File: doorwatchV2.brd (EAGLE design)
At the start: 91.4 x 77.5 mm, 43 parts, among them IC1 LM2576S-5.0, IC2 MAX3232CPE, K1 FINDER-43.61, Q1 IRLZ44Z, T1 BC847, T2 BC847, T3 BC847, T4 BC847, X1 MKDSN1,5/2-5,08, X2 D-SUB9-H2M09RA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

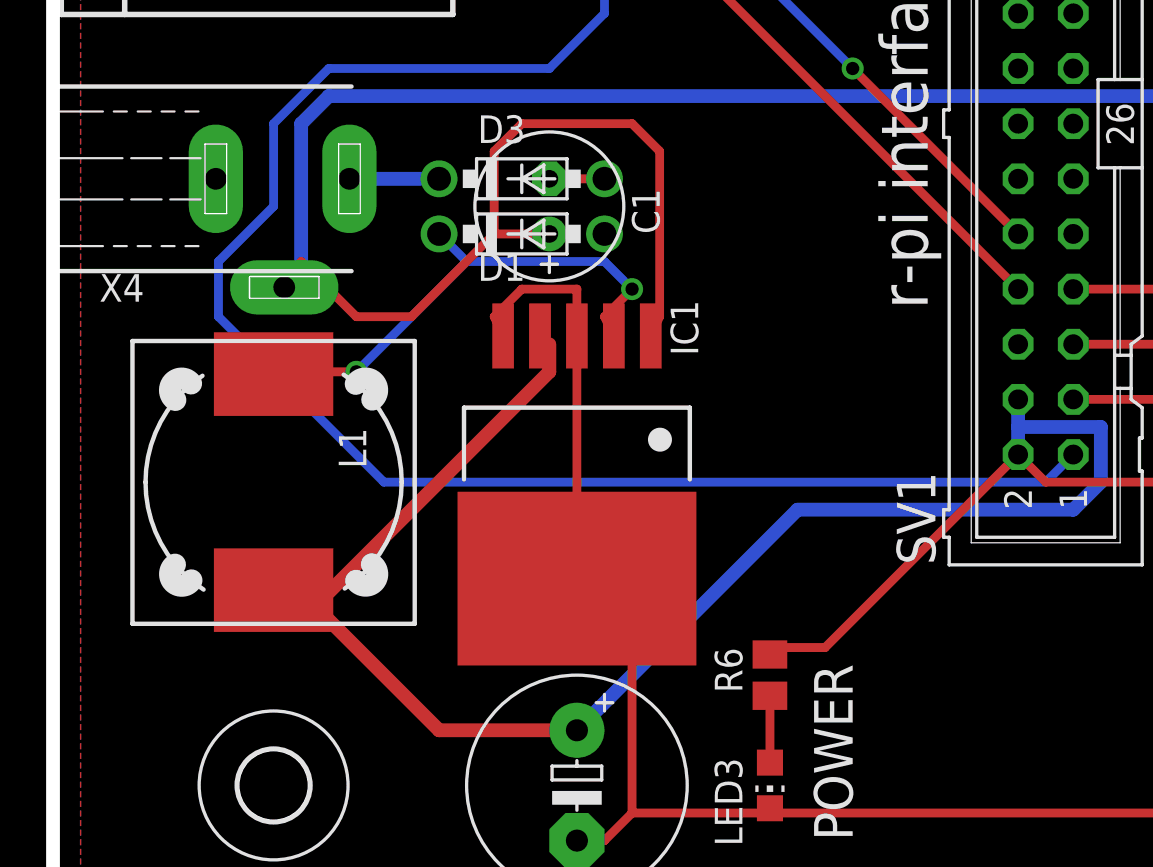
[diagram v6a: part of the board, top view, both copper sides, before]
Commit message: added reichelt.de warenkorb, package of inductive has been replaced, new routing of inductive and elko are necessary
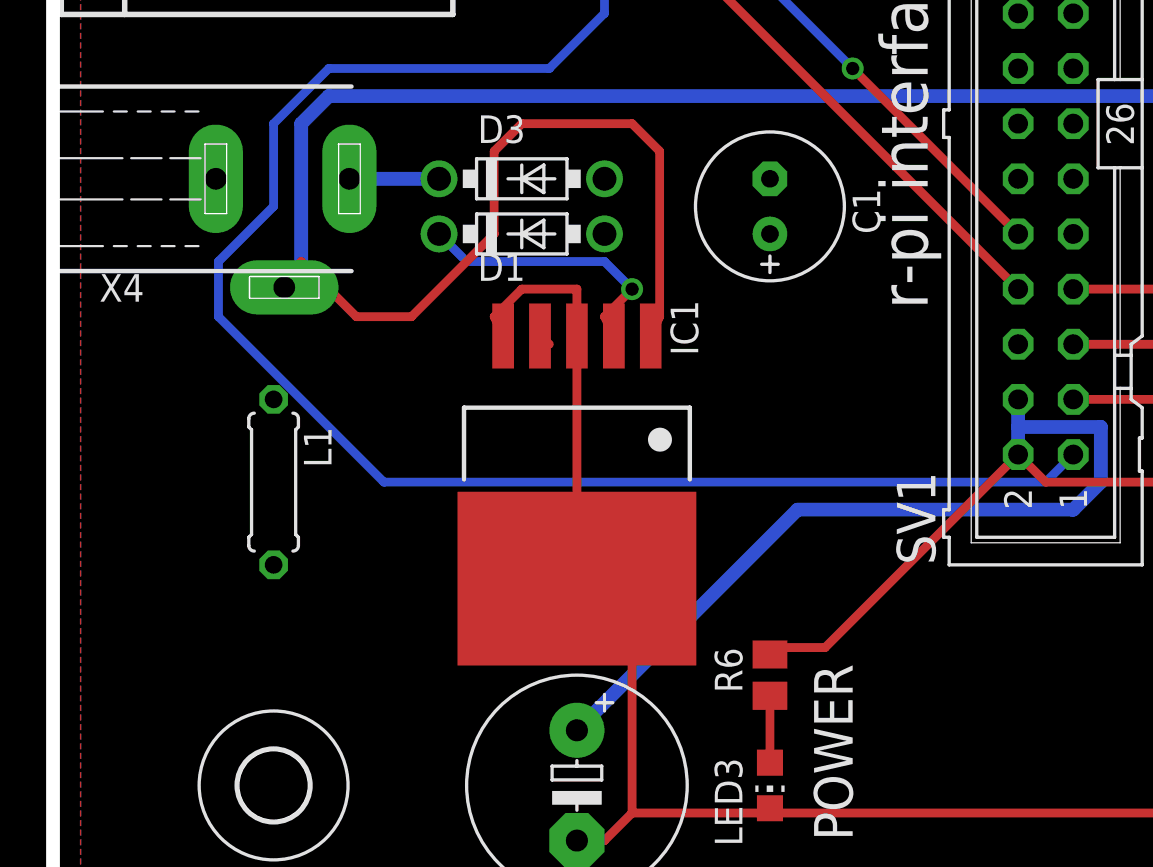
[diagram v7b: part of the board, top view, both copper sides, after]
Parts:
- L1: device inductors:DR125 -> rcl:0207/7
- moved C1 10.2 mm to (31.8, 59.7)
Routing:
- net +5V: track 112.4 -> 78.8 mm
- net N$3: track 23.8 -> 12.7 mm, vias 2 -> 1
- net GND: track 78.9 -> 76.4 mm
- net +12V: track 127.7 -> 125.1 mm
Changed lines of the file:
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@@
 <elements>
 <element name="IC1" library="regulators" package="TO263-5" value="LM2576S-5.0" x="22.86" y="45.72" rot="R180"/>
-<element name="L1" library="inductors" package="DR125" value="100uH" x="8.89" y="46.99" rot="R270"/>
+<element name="L1" library="rcl" package="0207/7" value="100uH" x="8.89" y="46.99" rot="R270"/>
 <element name="D1" library="diode" package="DO41-7.6" value="1N5817-B" x="20.32" y="58.42" smashed="yes">
 <attribute name="NAME" x="18.288" y="56.261" size="1.27" layer="25" ratio="10"/>
 <attribute name="VALUE" x="18.288" y="55.499" size="1.27" layer="27" ratio="10"/>
 </element>
-<element name="C1" library="rcl" package="E2,5-7" value="100uF" x="21.59" y="59.69" smashed="yes" rot="R90">
-<attribute name="NAME" x="26.67" y="58.42" size="1.27" layer="25" rot="R90"/>
-<attribute name="VALUE" x="24.13" y="58.42" size="1.27" layer="27" rot="R90"/>
+<element name="C1" library="rcl" package="E2,5-7" value="100uF" x="31.75" y="59.69" smashed="yes" rot="R90">
+<attribute name="NAME" x="36.83" y="58.42" size="1.27" layer="25" rot="R90"/>
+<attribute name="VALUE" x="34.29" y="58.42" size="1.27" layer="27" rot="R90"/>
 </element>
 <element name="C2" library="rcl" package="E5-10,5" value="1000uF" x="22.86" y="33.02" rot="R270"/>
@@
 <wire x1="60.96" y1="31.75" x2="60.96" y2="31.97" width="0.4064" layer="1"/>
 <wire x1="25.4" y1="31.75" x2="31.75" y2="31.75" width="0.4064" layer="1"/>
-<wire x1="24.13" y1="60.96" x2="21.59" y2="60.96" width="0.4064" layer="1"/>
+<wire x1="24.13" y1="60.96" x2="31.75" y2="60.96" width="0" layer="19" extent="1-16"/>
 <wire x1="31.75" y1="31.75" x2="54.61" y2="31.75" width="0.4064" layer="1"/>
 <wire x1="54.61" y1="31.75" x2="54.61" y2="31.97" width="0.4064" layer="1"/>
@@
 <signal name="N$3">
 <contactref element="IC1" pad="2"/>
-<contactref element="L1" pad="1"/>
 <contactref element="D1" pad="C"/>
 <wire x1="25.4" y1="55.88" x2="24.13" y2="54.61" width="0.4064" layer="1"/>
@@
 <wire x1="16.51" y1="58.42" x2="17.78" y2="57.15" width="0.4064" layer="16"/>
 <wire x1="24.13" y1="54.61" x2="24.56" y2="53.72" width="0.4064" layer="1"/>
-<wire x1="12.7" y1="52.07" x2="8.89" y2="52.07" width="0.4064" layer="1"/>
-<wire x1="17.78" y1="57.15" x2="12.7" y2="52.07" width="0.4064" layer="16"/>
-<wire x1="8.89" y1="52.07" x2="8.89" y2="51.965" width="0.4064" layer="1"/>
+<wire x1="12.7" y1="52.07" x2="8.89" y2="52.07" width="0" layer="19" extent="1-16"/>
+<wire x1="17.78" y1="57.15" x2="12.7" y2="52.07" width="0" layer="19" extent="1-16"/>
 <via x="25.4" y="55.88" extent="1-16" drill="0.6096"/>
-<via x="12.7" y="52.07" extent="1-16" drill="0.6096"/>
+<wire x1="12.7" y1="52.07" x2="12.7" y2="52.07" width="0" layer="19" extent="1-16"/>
+<contactref element="L1" pad="1"/>
+<wire x1="8.89" y1="50.8" x2="8.89" y2="52.07" width="0" layer="19" extent="1-1"/>
 </signal>
 <signal name="+5V">
-<contactref element="L1" pad="2"/>
 <contactref element="IC1" pad="4"/>
 <contactref element="C2" pad="+"/>
@@
 <contactref element="T4" pad="3"/>
 <contactref element="R6" pad="1"/>
-<wire x1="21.59" y1="52.07" x2="21.59" y2="53.34" width="0.635" layer="1"/>
-<wire x1="11.43" y1="41.91" x2="21.59" y2="52.07" width="0.635" layer="1"/>
-<wire x1="8.89" y1="41.91" x2="10.16" y2="41.91" width="0.4064" layer="1"/>
-<wire x1="10.16" y1="41.91" x2="11.43" y2="41.91" width="0.4064" layer="1"/>
+<wire x1="21.59" y1="52.07" x2="21.59" y2="53.34" width="0" layer="19" extent="1-16"/>
+<wire x1="11.43" y1="41.91" x2="21.59" y2="52.07" width="0" layer="19" extent="1-16"/>
+<wire x1="8.89" y1="41.91" x2="10.16" y2="41.91" width="0" layer="19" extent="1-16"/>
+<wire x1="10.16" y1="41.91" x2="11.43" y2="41.91" width="0" layer="19" extent="1-16"/>
 <wire x1="21.59" y1="53.34" x2="21.16" y2="53.72" width="0.4064" layer="1"/>
-<wire x1="8.89" y1="41.91" x2="8.89" y2="42.015" width="0.4064" layer="1"/>
 <wire x1="59.69" y1="50.8" x2="59.69" y2="46.99" width="0.4064" layer="1"/>
 <wire x1="59.69" y1="50.8" x2="59.69" y2="54.61" width="0.4064" layer="1"/>
 <wire x1="59.69" y1="54.61" x2="59.52" y2="54.61" width="0.4064" layer="1"/>
 <wire x1="59.69" y1="50.8" x2="59.52" y2="50.8" width="0.4064" layer="1"/>
-<wire x1="43.18" y1="48.26" x2="41.91" y2="46.99" width="0.4064" layer="1"/>
 <wire x1="31.75" y1="39.37" x2="31.75" y2="39.05" width="0.4064" layer="1"/>
 <wire x1="43.18" y1="48.26" x2="43.18" y2="49.53" width="0.635" layer="16"/>
@@
 <wire x1="46.99" y1="49.53" x2="46.99" y2="46.99" width="0.635" layer="16"/>
 <wire x1="43.18" y1="49.53" x2="46.99" y2="49.53" width="0.635" layer="16"/>
-<wire x1="10.16" y1="41.91" x2="16.51" y2="35.56" width="0.635" layer="1"/>
-<wire x1="16.51" y1="35.56" x2="22.86" y2="35.56" width="0.635" layer="1"/>
+<wire x1="10.16" y1="41.91" x2="16.51" y2="35.56" width="0" layer="19" extent="1-16"/>
+<wire x1="16.51" y1="35.56" x2="22.86" y2="35.56" width="0" layer="19" extent="1-16"/>
 <wire x1="31.75" y1="39.37" x2="34.29" y2="39.37" width="0.4064" layer="1"/>
-<wire x1="34.29" y1="39.37" x2="41.91" y2="46.99" width="0.4064" layer="1"/>
+<wire x1="34.29" y1="39.37" x2="43.18" y2="48.26" width="0.4064" layer="1"/>
+<contactref element="L1" pad="2"/>
+<wire x1="8.89" y1="41.91" x2="8.89" y2="43.18" width="0" layer="19" extent="1-1"/>
 </signal>
 <signal name="+3V3">
@@
 <contactref element="OK1" pad="8"/>
 <contactref element="T3" pad="3"/>
-<wire x1="19.05" y1="58.42" x2="21.59" y2="58.42" width="0.4064" layer="1"/>
+<wire x1="19.05" y1="58.42" x2="31.75" y2="58.42" width="0" layer="19" extent="1-16"/>
 <wire x1="15.24" y1="54.61" x2="19.05" y2="58.42" width="0.4064" layer="1"/>
 <wire x1="12.7" y1="54.61" x2="15.24" y2="54.61" width="0.4064" layer="1"/>

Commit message: updated board
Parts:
- L1: device rcl:0207/7 -> rcl:0207/12
- moved L1 5.24 mm to (14.0, 45.7)
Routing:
- net +5V: track 78.8 -> 106.0 mm
- net N$3: track 12.7 -> 22.5 mm, vias 1 -> 0
- net GND: track 76.4 -> 83.3 mm
- net +12V: track 125.1 -> 131.0 mm
- net +3V3: track 78.3 -> 77.5 mm
